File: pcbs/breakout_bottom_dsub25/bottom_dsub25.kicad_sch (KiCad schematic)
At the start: 5 parts, among them J1 DB25_Pins, J4 Screw_Terminal_01x06, J5 Screw_Terminal_01x06, J8_Z1 Conn_01x06_Pin, J8_Z2 Conn_01x06_Pin

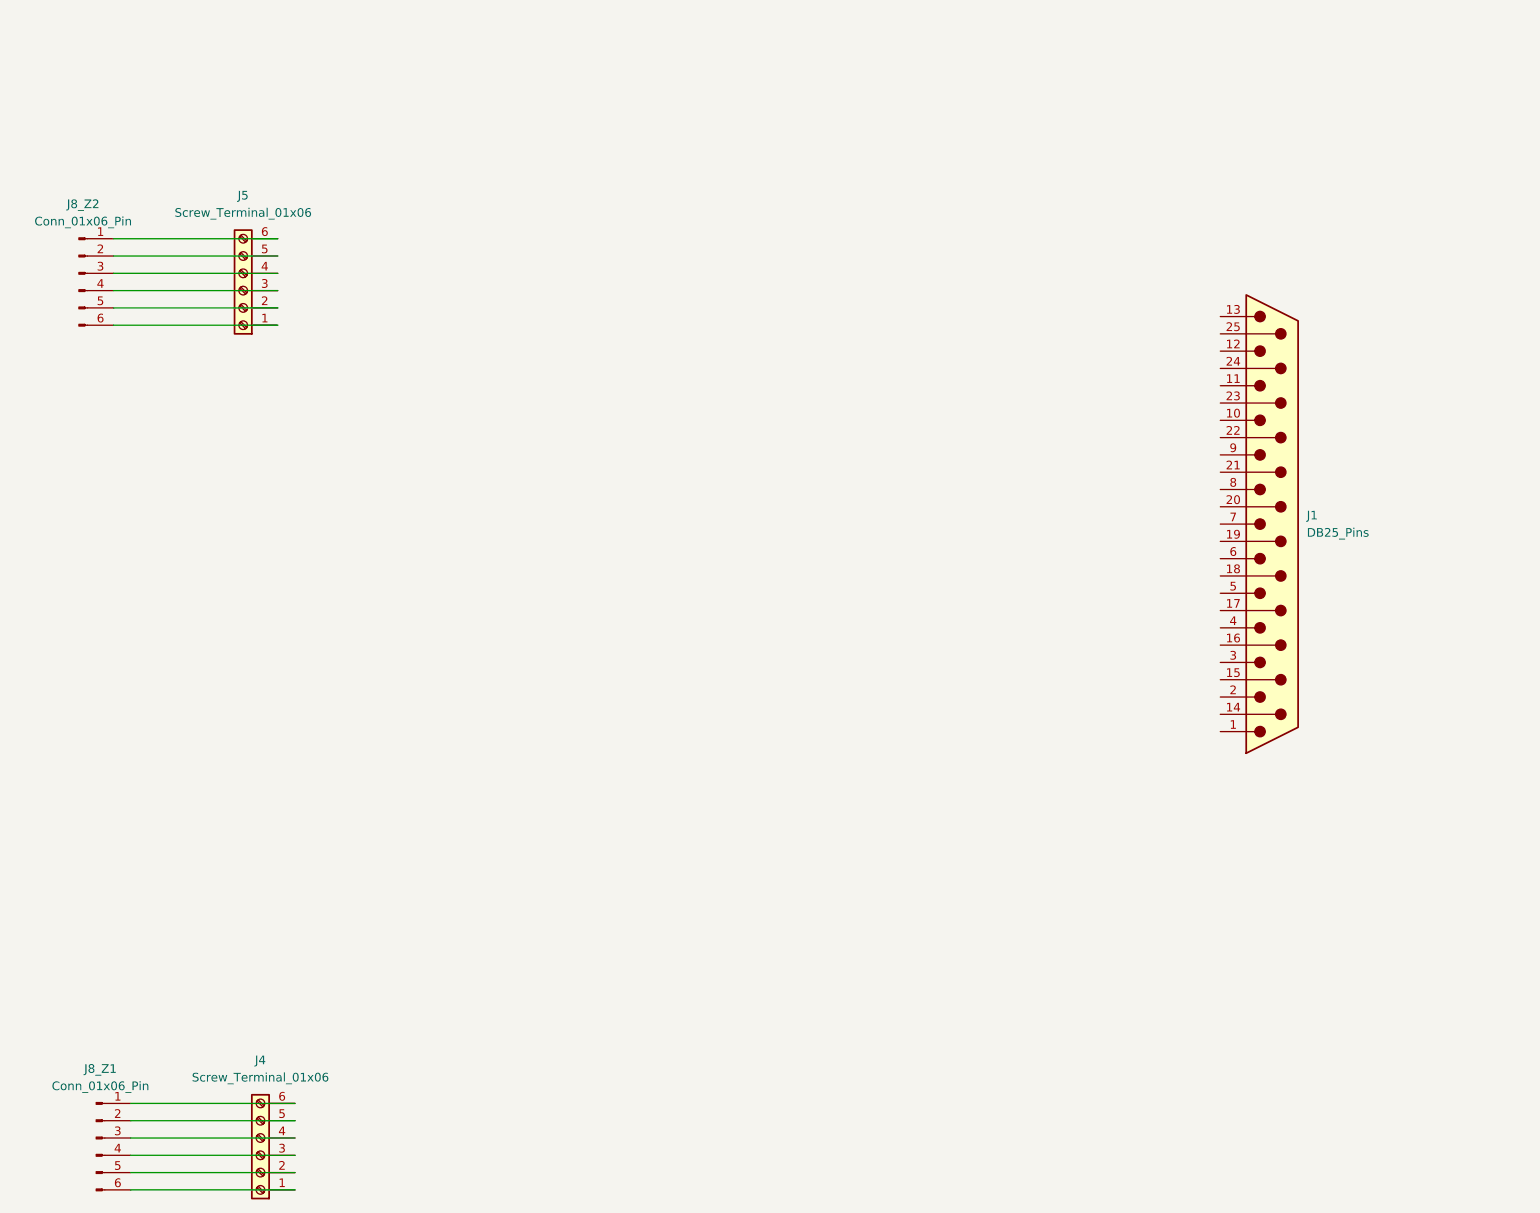
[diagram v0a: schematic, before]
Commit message: progress on the bottom board (most connectors, etc)
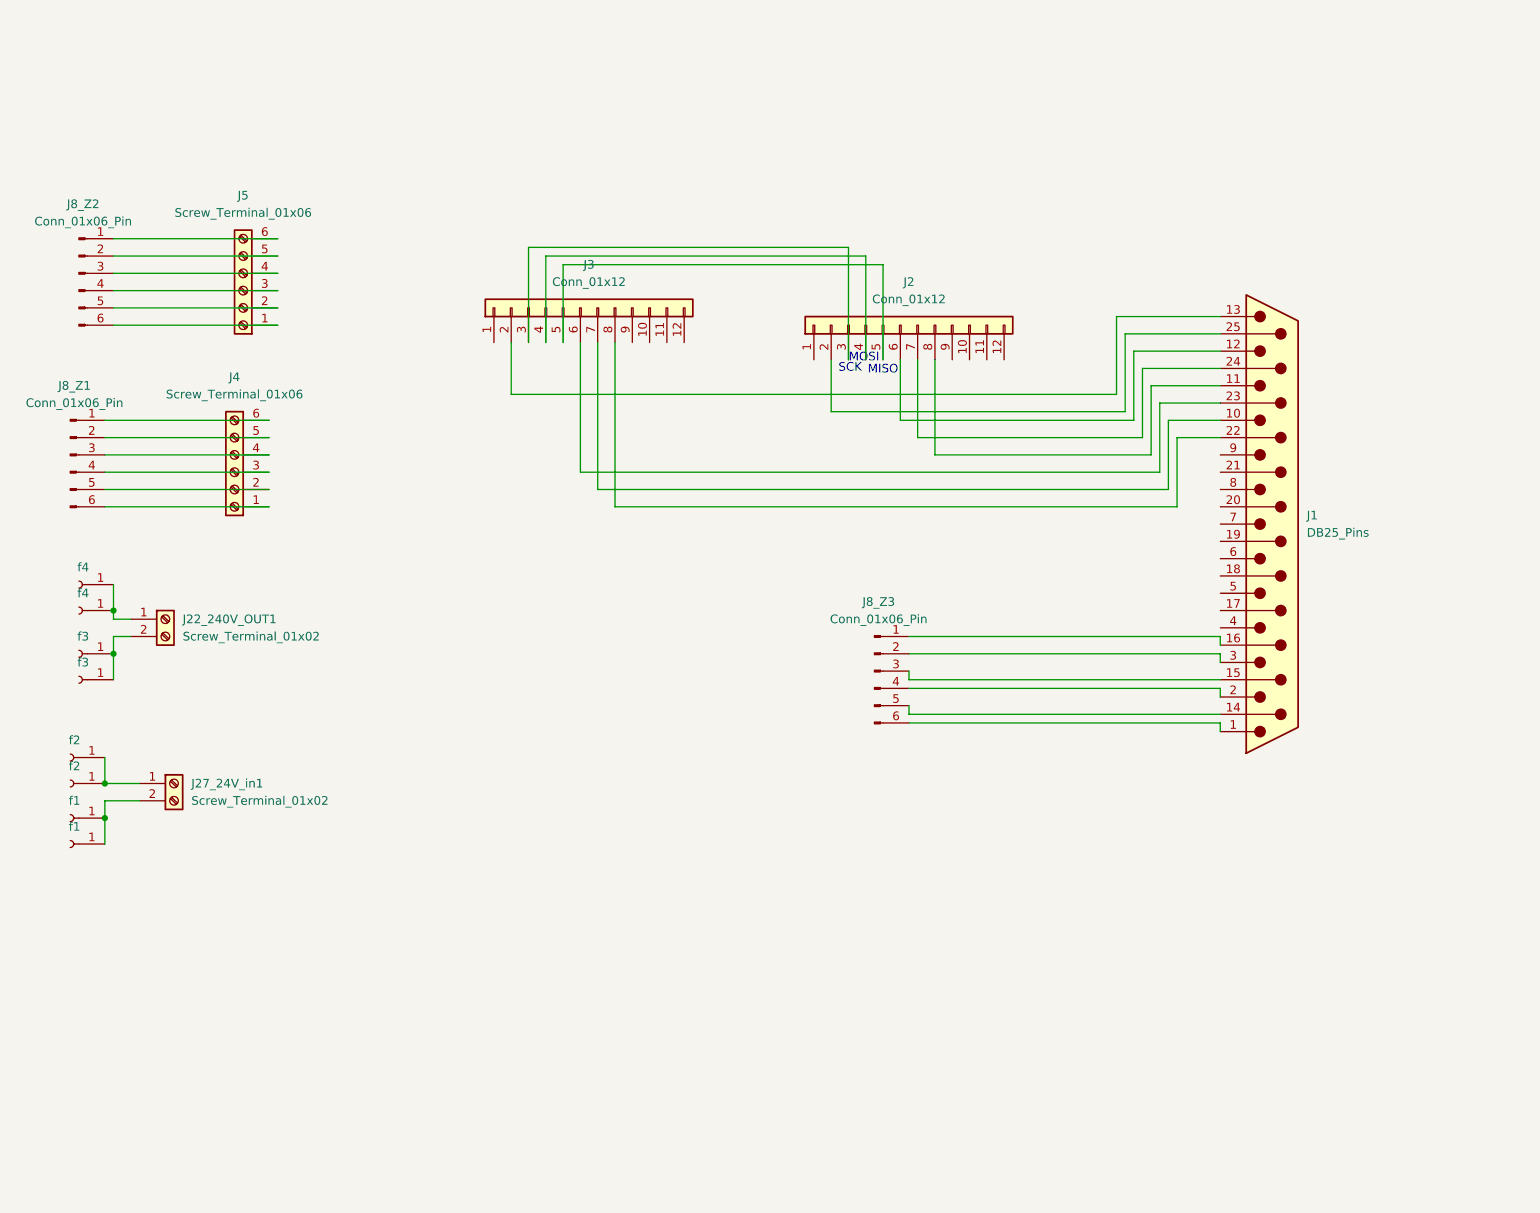
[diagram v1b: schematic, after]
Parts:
- added J10, J11: f3, Connector_Wire:SolderWire-1.5sqmm_1x01_D1.7mm_OD3mm, symbol Connector:Conn_01x01_Socket
- added J12, J16: f4, Connector_Wire:SolderWire-1.5sqmm_1x01_D1.7mm_OD3mm, symbol Connector:Conn_01x01_Socket
- added J2, J3: Conn_01x12, Connector_JST:JST_ZH_B12B-ZR_1x12_P1.50mm_Vertical, symbol Connector_Generic:Conn_01x12
- added J22_240V_OUT1, J27_24V_in1: Screw_Terminal_01x02, TerminalBlock_Phoenix:TerminalBlock_Phoenix_MKDS-1-2-3.81_1x02_P3.81mm_Horizontal, symbol Connector:Screw_Terminal_01x02
- added J23, J24: f2, Connector_Wire:SolderWire-1.5sqmm_1x01_D1.7mm_OD3mm, symbol Connector:Conn_01x01_Socket
- added J25, J26: f1, Connector_Wire:SolderWire-1.5sqmm_1x01_D1.7mm_OD3mm, symbol Connector:Conn_01x01_Socket
- added J8_Z3: Conn_01x06_Pin, Connector_JST:JST_XA_S06B-XASK-1_1x06_P2.50mm_Horizontal, symbol Connector:Conn_01x06_Pin
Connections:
- net at J1.1: now also J8_Z3.6 (Pin_6)
- net at J1.10: now also J3.7 (Pin_7)
- net at J1.11: now also J2.8 (Pin_8)
- net at J1.12: now also J2.6 (Pin_6)
- net at J1.13: now also J3.2 (Pin_2)
- net at J1.14 (P14): now also J8_Z3.5 (Pin_5)
- net at J1.15 (P15): now also J8_Z3.3 (Pin_3)
- net at J1.16 (P16): now also J8_Z3.1 (Pin_1)
- net at J1.2: now also J8_Z3.4 (Pin_4)
- net at J1.22 (P22): now also J3.8 (Pin_8)
- net at J1.23 (P23): now also J3.6 (Pin_6)
- net at J1.24 (P24): now also J2.7 (Pin_7)
- net at J1.25 (P25): now also J2.2 (Pin_2)
- net at J1.3: now also J8_Z3.2 (Pin_2)
- new net: J23.1 (Pin_1), J24.1 (Pin_1), J27_24V_in1.1 (Pin_1)
- new net: J25.1 (Pin_1), J26.1 (Pin_1), J27_24V_in1.2 (Pin_2)
- new net: J12.1 (Pin_1), J16.1 (Pin_1), J22_240V_OUT1.1 (Pin_1)
- new net: J10.1 (Pin_1), J11.1 (Pin_1), J22_240V_OUT1.2 (Pin_2)
- new net: J2.3 (Pin_3), J3.3 (Pin_3)
- new net: J2.4 (Pin_4), J3.4 (Pin_4)
- new net: J2.5 (Pin_5), J3.5 (Pin_5)
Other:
- note added: "MISO"
- note added: "MOSI"
- note added: "SCK"
- moved on the sheet: J4, J8_Z1

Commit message: rough component positioning for bottom pcb + add connectors
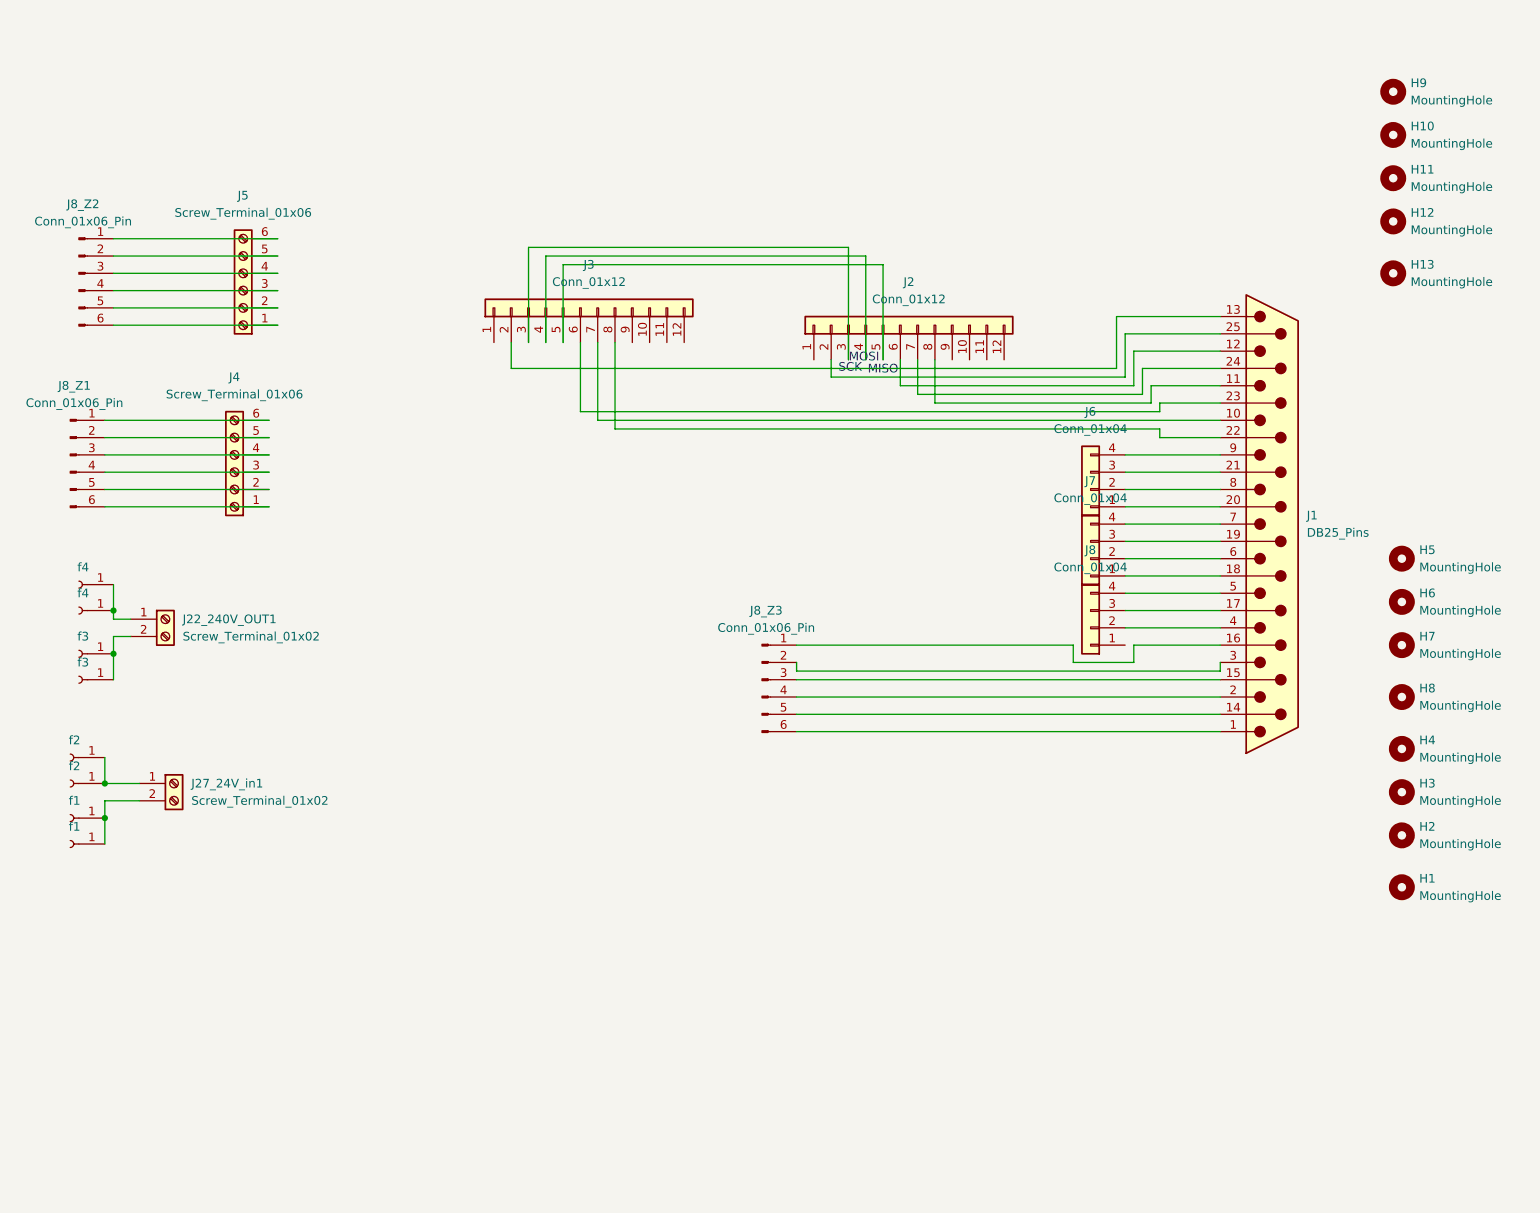
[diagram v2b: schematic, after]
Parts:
- added H1, H2, H3, H4, H5, H6, H7, H8: MountingHole, MountingHole:MountingHole_3.2mm_M3_DIN965_Pad_TopBottom, symbol Mechanical:MountingHole
- added H10, H11, H12, H13, H9: MountingHole, MountingHole:MountingHole_4.3mm_M4_DIN965_Pad_TopBottom, symbol Mechanical:MountingHole
- added J6, J7, J8: Conn_01x04, Connector_JST:JST_XH_B4B-XH-A_1x04_P2.50mm_Vertical, symbol Connector_Generic:Conn_01x04
- J8_Z1, J8_Z2: footprint Connector_JST:JST_XA_S06B-XASK-1_1x06_P2.50mm_Horizontal -> Connector_JST:JST_VH_B6PS-VH_1x06_P3.96mm_Horizontal
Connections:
- net at J1.17 (P17): now also J8.3 (Pin_3)
- net at J1.18 (P18): now also J7.1 (Pin_1)
- net at J1.19 (P19): now also J7.3 (Pin_3)
- net at J1.20 (P20): now also J6.1 (Pin_1)
- net at J1.21 (P21): now also J6.3 (Pin_3)
- net at J1.4: now also J8.2 (Pin_2)
- net at J1.5: now also J8.4 (Pin_4)
- net at J1.6: now also J7.2 (Pin_2)
- net at J1.7: now also J7.4 (Pin_4)
- net at J1.8: now also J6.2 (Pin_2)
- net at J1.9: now also J6.4 (Pin_4)
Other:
- moved on the sheet: J8_Z3

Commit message: add routinng
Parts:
- removed J10, J11: f3, Connector_Wire:SolderWire-1.5sqmm_1x01_D1.7mm_OD3mm, symbol Connector:Conn_01x01_Socket
- removed J12, J16: f4, Connector_Wire:SolderWire-1.5sqmm_1x01_D1.7mm_OD3mm, symbol Connector:Conn_01x01_Socket
- removed J22_240V_OUT1, J27_24V_in1: Screw_Terminal_01x02, TerminalBlock_Phoenix:TerminalBlock_Phoenix_MKDS-1-2-3.81_1x02_P3.81mm_Horizontal, symbol Connector:Screw_Terminal_01x02
- removed J23, J24: f2, Connector_Wire:SolderWire-1.5sqmm_1x01_D1.7mm_OD3mm, symbol Connector:Conn_01x01_Socket
- removed J25, J26: f1, Connector_Wire:SolderWire-1.5sqmm_1x01_D1.7mm_OD3mm, symbol Connector:Conn_01x01_Socket
- removed J6: Conn_01x04, Connector_JST:JST_XH_B4B-XH-A_1x04_P2.50mm_Vertical, symbol Connector_Generic:Conn_01x04
- J1: footprint Connector_Dsub:DSUB-25_Pins_Horizontal_P2.77x2.54mm_EdgePinOffset9.40mm -> Connector_Dsub:DSUB-25_Pins_Vertical_P2.77x2.84mm_MountingHoles
- J8_Z1, J8_Z2: footprint Connector_JST:JST_VH_B6PS-VH_1x06_P3.96mm_Horizontal -> Connector_JST:JST_VH_B6P-VH_1x06_P3.96mm_Vertical
- J8_Z3: footprint Connector_JST:JST_XA_S06B-XASK-1_1x06_P2.50mm_Horizontal -> Connector_JST:JST_XA_B06B-XASK-1_1x06_P2.50mm_Vertical
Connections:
- net at J1.10: now also J2.3 (Pin_3), J3.3 (Pin_3); no longer J3.7 (Pin_7)
- net at J1.11: now also J2.5 (Pin_5), J3.5 (Pin_5); no longer J2.8 (Pin_8)
- net at J1.12: now also J2.7 (Pin_7); no longer J2.6 (Pin_6)
- net at J3.2 (Pin_2): now also J1.9; no longer J1.13
- net at J1.20 (P20): now also J3.8 (Pin_8)
- net at J1.21 (P21): now also J3.6 (Pin_6)
- net at J1.22 (P22): now also J2.2 (Pin_2); no longer J3.8 (Pin_8)
- net at J1.23 (P23): now also J2.4 (Pin_4), J3.4 (Pin_4); no longer J3.6 (Pin_6)
- net at J1.24 (P24): now also J2.6 (Pin_6); no longer J2.7 (Pin_7)
- net at J1.25 (P25): now also J2.8 (Pin_8); no longer J2.2 (Pin_2)
- net at J1.8: now also J3.7 (Pin_7)
- net GND: now reaches J2.9 (Pin_9)
- net GND: now also J1.13, J3.9 (Pin_9)
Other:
- note removed: "MISO"
- note removed: "MOSI"
- note removed: "SCK"
- moved on the sheet: J7, J8, J8_Z3

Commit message: adding various silk layer labels
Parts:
- added FID1, FID2, FID3: Fiducial, symbol Mechanical:Fiducial
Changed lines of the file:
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@@
+	)
+	(symbol
+		(lib_id "Mechanical:Fiducial")
+		(at 266.7 20.32 0)
+		(unit 1)
+		(body_style 1)
+		(exclude_from_sim no)
+		(in_bom no)
+		(on_board yes)
+		(in_pos_files yes)
+		(dnp no)
+		(fields_autoplaced yes)
+		(property "Reference" "FID3"
+			(at 269.24 19.0499 0)
+			(show_name no)
+			(do_not_autoplace no)
+			(effects
+				(font
+					(size 1.27 1.27)
+				)
+				(justify left)
+			)
+		)
+		(property "Value" "Fiducial"
+			(at 269.24 21.5899 0)
+			(show_name no)
+			(do_not_autoplace no)
+			(effects
+				(font
+					(size 1.27 1.27)
+				)
+				(justify left)
+			)
+		)
+		(property "Footprint" ""
+			(at 266.7 20.32 0)
+			(hide yes)
+			(show_name no)
+			(do_not_autoplace no)
+			(effects
+				(font
+					(size 1.27 1.27)
+				)
+			)
+		)
+		(property "Datasheet" ""
+			(at 266.7 20.32 0)
+			(hide yes)
+			(show_name no)
+			(do_not_autoplace no)
+			(effects
+				(font
+					(size 1.27 1.27)
+				)
+			)
+		)
+		(property "Description" "Fiducial Marker"
+			(at 266.7 20.32 0)
+			(hide yes)
+			(show_name no)
+			(do_not_autoplace no)
+			(effects
+				(font
+					(size 1.27 1.27)
+				)
+			)
+		)
+		(instances
+			(project "bottom_dsub25"
+				(path "/36cdabbf-675f-46a3-8745-6c7471a8ba73"
+					(reference "FID3")
+					(unit 1)
+				)
+			)
+		)
 	)
 	(symbol
@@
 	)
 	(symbol
+		(lib_id "Mechanical:Fiducial")
+		(at 218.44 20.32 0)
+		(unit 1)
+		(body_style 1)
+		(exclude_from_sim no)
+		(in_bom no)
+		(on_board yes)
+		(in_pos_files yes)
+		(dnp no)
+		(fields_autoplaced yes)
+		(property "Reference" "FID1"
+			(at 220.98 19.0499 0)
+			(show_name no)
+			(do_not_autoplace no)
+			(effects
+				(font
+					(size 1.27 1.27)
+				)
+				(justify left)
+			)
+		)
+		(property "Value" "Fiducial"
+			(at 220.98 21.5899 0)
+			(show_name no)
+			(do_not_autoplace no)
+			(effects
+				(font
+					(size 1.27 1.27)
+				)
+				(justify left)
+			)
+		)
+		(property "Footprint" ""
+			(at 218.44 20.32 0)
+			(hide yes)
+			(show_name no)
+			(do_not_autoplace no)
+			(effects
+				(font
+					(size 1.27 1.27)
+				)
+			)
+		)
+		(property "Datasheet" ""
+			(at 218.44 20.32 0)
+			(hide yes)
+			(show_name no)
+			(do_not_autoplace no)
+			(effects
+				(font
+					(size 1.27 1.27)
+				)
+			)
+		)
+		(property "Description" "Fiducial Marker"
+			(at 218.44 20.32 0)
+			(hide yes)
+			(show_name no)
+			(do_not_autoplace no)
+			(effects
+				(font
+					(size 1.27 1.27)
+				)
+			)
+		)
+		(instances
+			(project "bottom_dsub25"
+				(path "/36cdabbf-675f-46a3-8745-6c7471a8ba73"
+					(reference "FID1")
+					(unit 1)
+				)
+			)
+		)
+	)
+	(symbol
 		(lib_id "power:GND")
 		(at 153.67 66.04 0)
@@
 					(unit 1)
 				)
+			)
+		)
+	)
+	(symbol
+		(lib_id "Mechanical:Fiducial")
+		(at 241.3 20.32 0)
+		(unit 1)
+		(body_style 1)
+		(exclude_from_sim no)
+		(in_bom no)
+		(on_board yes)
+		(in_pos_files yes)
+		(dnp no)
+		(fields_autoplaced yes)
+		(property "Reference" "FID2"
+			(at 243.84 19.0499 0)
+			(show_name no)
+			(do_not_autoplace no)
+			(effects
+				(font
+					(size 1.27 1.27)
+				)
+				(justify left)
+			)
+		)
+		(property "Value" "Fiducial"
+			(at 243.84 21.5899 0)
+			(show_name no)
+			(do_not_autoplace no)
+			(effects
+				(font
+					(size 1.27 1.27)
+				)
+				(justify left)
+			)
+		)
+		(property "Footprint" ""
+			(at 241.3 20.32 0)
+			(hide yes)
+			(show_name no)
+			(do_not_autoplace no)
+			(effects
+				(font
+					(size 1.27 1.27)
+				)
+			)
+		)
+		(property "Datasheet" ""
+			(at 241.3 20.32 0)
+			(hide yes)
+			(show_name no)
+			(do_not_autoplace no)
+			(effects
+				(font
+					(size 1.27 1.27)
+				)
+			)
+		)
+		(property "Description" "Fiducial Marker"
+			(at 241.3 20.32 0)
+			(hide yes)
+			(show_name no)
+			(do_not_autoplace no)
+			(effects
+				(font
+					(size 1.27 1.27)
+				)
+			)
+		)
+		(instances
+			(project "bottom_dsub25"
+				(path "/36cdabbf-675f-46a3-8745-6c7471a8ba73"
+					(reference "FID2")
+					(unit 1)
+				)
